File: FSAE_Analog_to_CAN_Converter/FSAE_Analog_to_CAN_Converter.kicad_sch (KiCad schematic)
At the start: 31 parts, among them J1 Conn_01x05_Pin, J2 Conn_01x08_Pin, J3 Conn_01x02_Pin, U1 STM32F103RCTx, U2 AP63205WU, U3 MCP2561-E-MF, U4 LT1962-3.3

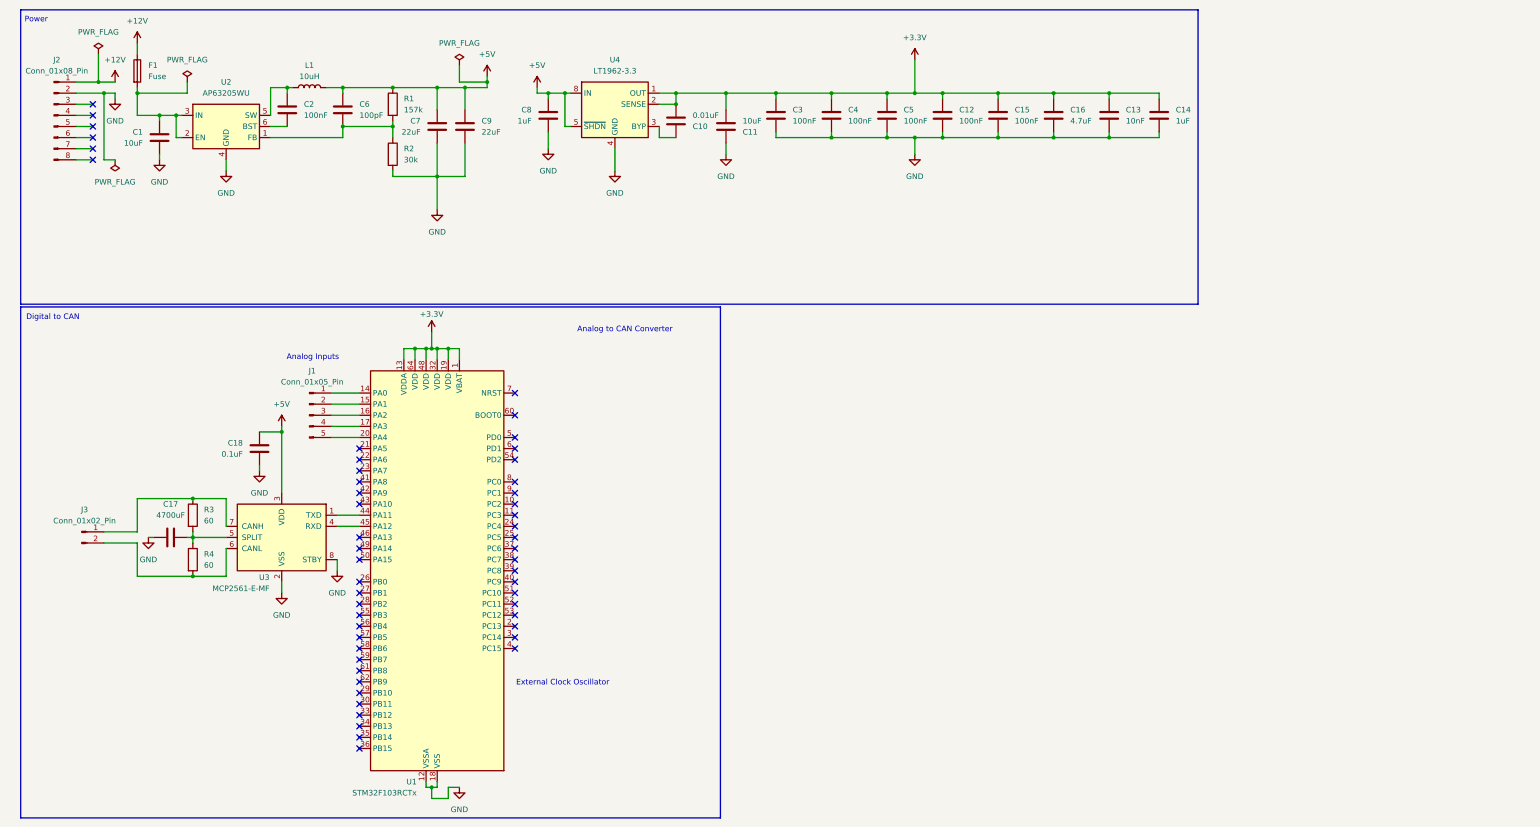
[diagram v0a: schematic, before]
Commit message: assigned footprints
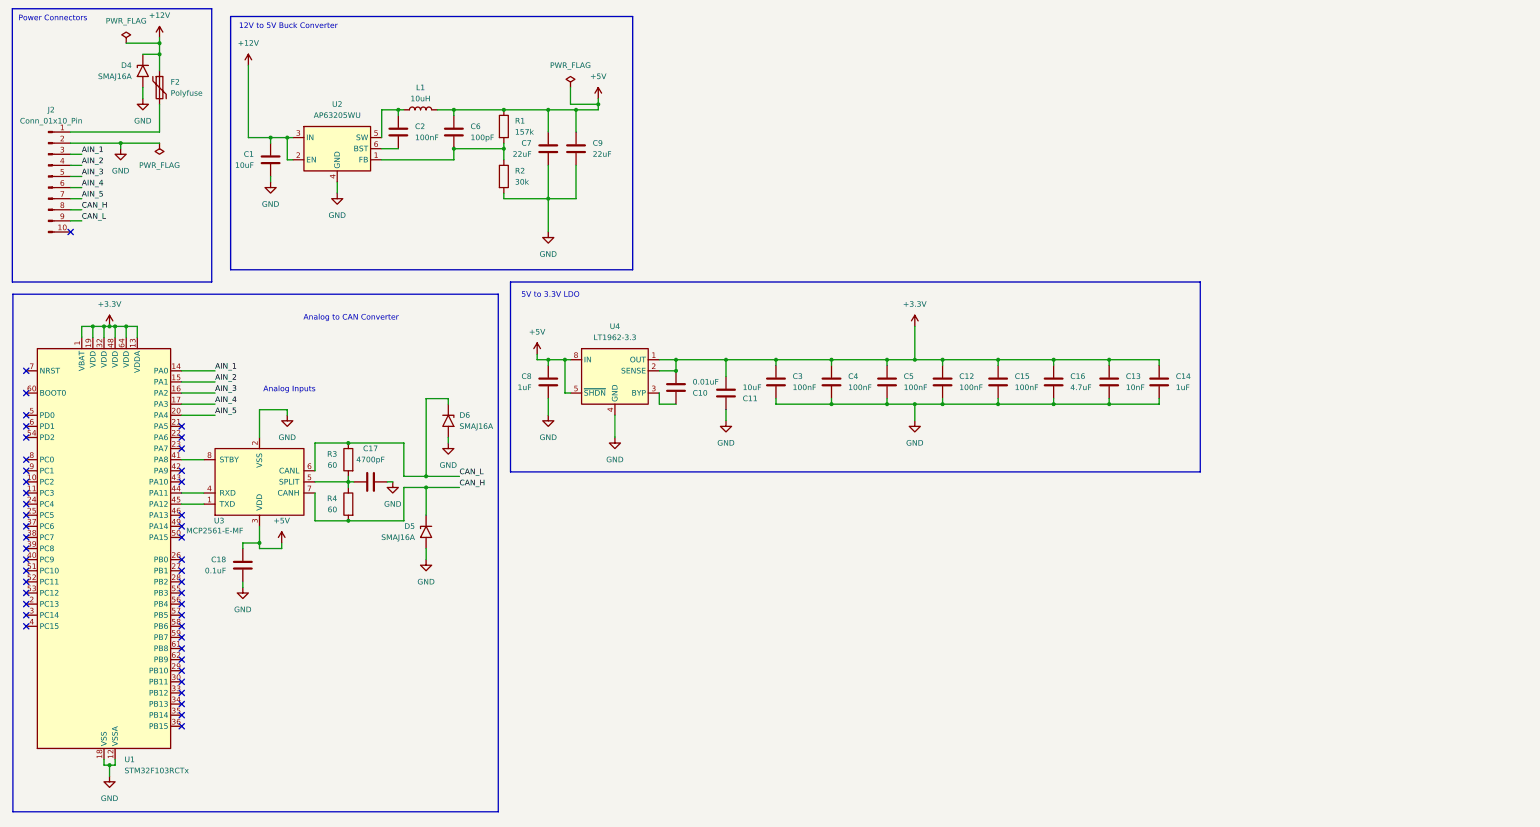
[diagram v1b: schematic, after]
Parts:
- removed F1: Fuse, symbol Device:Fuse
- removed J1: Conn_01x05_Pin, symbol Connector:Conn_01x05_Pin
- removed J2: Conn_01x08_Pin, symbol Connector:Conn_01x08_Pin
- removed J3: Conn_01x02_Pin, symbol Connector:Conn_01x02_Pin
- added D4, D5, D6: SMAJ16A, Diode_SMD:D_SMA, symbol Diode:SMAJ16A
- added F2: Polyfuse, Fuse:Fuse_1812_4532Metric_Pad1.30x3.40mm_HandSolder, symbol Device:Polyfuse
- added J2: Conn_01x10_Pin, Connector_Molex:Molex_KK-254_AE-6410-10A_1x10_P2.54mm_Vertical, symbol Connector:Conn_01x10_Pin
- C1, C10, C11, C12, C13, C14, C15, C16, C18, C2, C3, C4, C5, C6, C7, C8, C9: footprint (none) -> Capacitor_SMD:C_0603_1608Metric_Pad1.08x0.95mm_HandSolder
- C17: value 4700uF -> 4700pF; footprint (none) -> Capacitor_SMD:C_0603_1608Metric_Pad1.08x0.95mm_HandSolder
- L1: footprint (none) -> Inductor_SMD:L_0201_0603Metric_Pad0.64x0.40mm_HandSolder
- R1, R2, R3, R4: footprint (none) -> Resistor_SMD:R_0201_0603Metric_Pad0.64x0.40mm_HandSolder
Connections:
- net +12V: now also C1.1, U2.2 (EN), U2.3 (IN), D4.1 (A1), F2.1
- net GND: now also D4.2 (A2), D5.2 (A2), D6.2 (A2), J2.2 (Pin_2); no longer U3.8 (STBY)
- net CAN_H: now reaches U3.7 (CANH)
- net CAN_H: now also R4.2, D5.1 (A1), J2.8 (Pin_8); no longer R3.1
- net CAN_L: now reaches U3.6 (CANL)
- net CAN_L: now also R3.1, D6.1 (A1), J2.9 (Pin_9); no longer R4.2
- net AIN_1: now reaches U1.14 (PA0)
- net AIN_1: now also J2.3 (Pin_3)
- net AIN_2: now reaches U1.15 (PA1)
- net AIN_2: now also J2.4 (Pin_4)
- net AIN_3: now reaches U1.16 (PA2)
- net AIN_3: now also J2.5 (Pin_5)
- net AIN_4: now reaches U1.17 (PA3)
- net AIN_4: now also J2.6 (Pin_6)
- net AIN_5: now reaches U1.20 (PA4)
- net AIN_5: now also J2.7 (Pin_7)
- net at U1.41 (PA8): now also U3.8 (STBY)
- net at U1.44 (PA11): now also U3.4 (RXD); no longer U3.1 (TXD)
- net at U1.45 (PA12): now also U3.1 (TXD); no longer U3.4 (RXD)
- new net: F2.2, J2.1 (Pin_1)
- no-connect marks 52 -> 46
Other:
- note added: "12V to 5V Buck Converter"
- note added: "5V to 3.3V LDO"
- note added: "Power Connectors"
- note removed: "Digital to CAN"
- note removed: "External Clock Oscillator"
- note removed: "Power"
- moved on the sheet: C1, C10, C11, C12, C13, C14, C15, C16, C17, C18, C2, C3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

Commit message: started layout and traces
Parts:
- J1: renamed from J2; footprint Connector_Molex:Molex_KK-254_AE-6410-10A_1x10_P2.54mm_Vertical -> Connector_Molex:Molex_Mini-Fit_Jr_5566-10A_2x05_P4.20mm_Vertical
- L1: footprint Inductor_SMD:L_0201_0603Metric_Pad0.64x0.40mm_HandSolder -> Inductor_SMD:L_1210_3225Metric_Pad1.42x2.65mm_HandSolder
- renumbered C18 to C1, C11 to C10, C3 to C11, C4 to C12, C5 to C13, C12 to C14, C13 to C17, C14 to C18, C1 to C2, C17 to C3, C2 to C4, C6 to C5, C7 to C6, C8 to C7, C9 to C8, C10 to C9, D4 to D1, D5 to D2, D6 to D3, F2 to F1, R3 to R1, R4 to R2, R1 to R3, R2 to R4, U3 to U2, U2 to U3

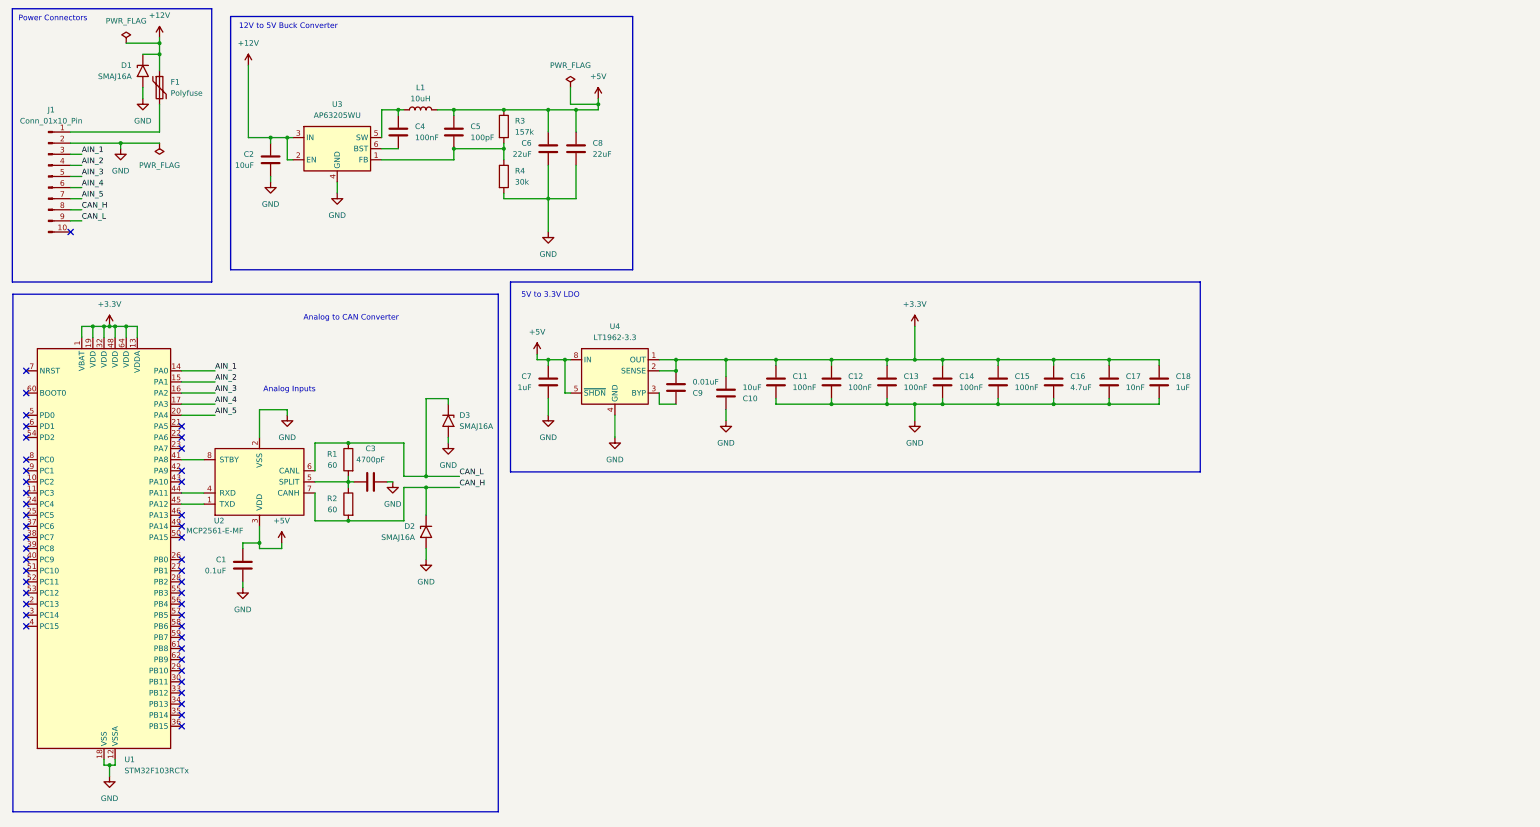
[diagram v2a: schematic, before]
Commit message: added external clock, and SWD output header
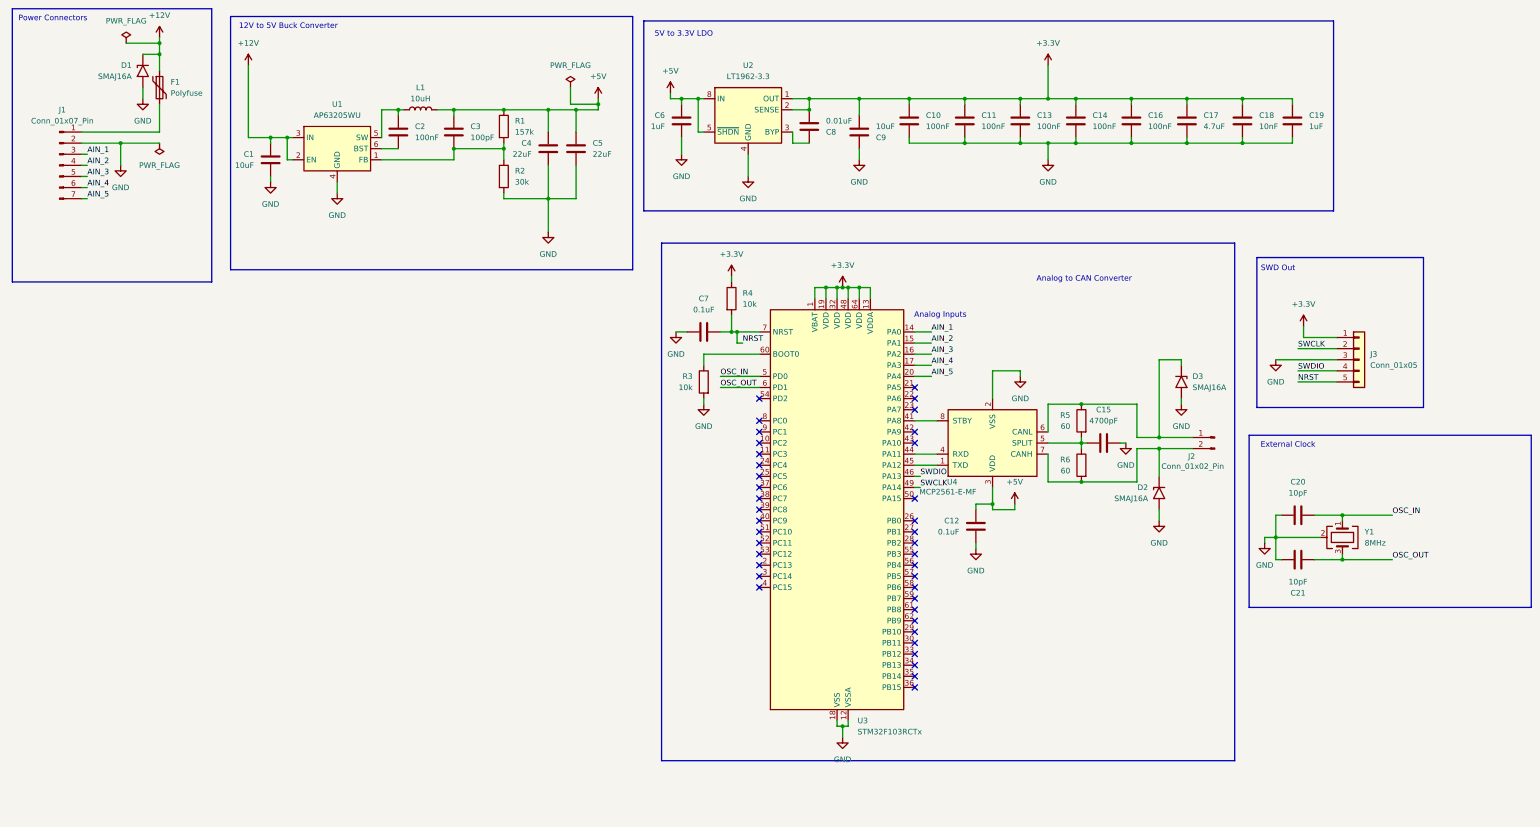
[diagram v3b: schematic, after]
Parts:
- removed J1: Conn_01x10_Pin, Connector_Molex:Molex_Mini-Fit_Jr_5566-10A_2x05_P4.20mm_Vertical, symbol Connector:Conn_01x10_Pin
- added C20, C21: 10pF, Capacitor_SMD:C_0603_1608Metric_Pad1.08x0.95mm_HandSolder, symbol Device:C
- added C7: 0.1uF, Capacitor_SMD:C_0603_1608Metric_Pad1.08x0.95mm_HandSolder, symbol Device:C
- added J1: Conn_01x07_Pin, Connector_Molex:Molex_Micro-Fit_3.0_43650-0700_1x07_P3.00mm_Horizontal, symbol Connector:Conn_01x07_Pin
- added J2: Conn_01x02_Pin, Connector_Molex:Molex_Micro-Fit_3.0_43650-0200_1x02_P3.00mm_Horizontal, symbol Connector:Conn_01x02_Pin
- added J3: Conn_01x05, Connector_PinHeader_2.54mm:PinHeader_1x05_P2.54mm_Vertical, symbol Connector_Generic:Conn_01x05
- added R3, R4: 10k, Resistor_SMD:R_0201_0603Metric_Pad0.64x0.40mm_HandSolder, symbol Device:R
- added Y1: 8MHz, Crystal:Crystal_SMD_3225-4Pin_3.2x2.5mm_HandSoldering, symbol Device:Crystal_GND24
- renumbered C2 to C1, C11 to C10, C12 to C11, C1 to C12, C3 to C15, C15 to C16, C16 to C17, C17 to C18, C18 to C19, C4 to C2, C5 to C3, C6 to C4, C8 to C5, C7 to C6, C9 to C8, C10 to C9, R3 to R1, R4 to R2, R1 to R5, R2 to R6, U3 to U1, U4 to U2, U1 to U3, U2 to U4
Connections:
- net +3.3V: now also J3.1 (Pin_1), R4.1
- net AIN_1: now also J1.3 (Pin_3)
- net AIN_2: now also J1.4 (Pin_4)
- net AIN_3: now also J1.5 (Pin_5)
- net AIN_4: now also J1.6 (Pin_6)
- net AIN_5: now also J1.7 (Pin_7)
- net GND: now also C20.1, C21.1, C7.1, J1.2 (Pin_2), J3.3 (Pin_3), R3.2, Y1.2 (G), Y1.4 (G)
- net SWDIO: now reaches U3.46 (PA13)
- net SWDIO: now also J3.4 (Pin_4)
- net SWCLK: now reaches U3.49 (PA14)
- net SWCLK: now also J3.2 (Pin_2)
- net OSC_IN: now reaches U3.5 (PD0)
- net OSC_IN: now also C20.2, Y1.1
- net OSC_OUT: now reaches U3.6 (PD1)
- net OSC_OUT: now also C21.2, Y1.3
- net at U3.60 (BOOT0): now also R3.1
- net NRST: now reaches U3.7 (NRST)
- net NRST: now also C7.2, J3.5 (Pin_5), R4.2
- net at F1.2: now also J1.1 (Pin_1)
- net CAN_H: no longer names the net of D2.1 (A1), R6.2, U4.7 (CANH)
- net CAN_H: now also J2.2 (Pin_2)
- net CAN_L: no longer names the net of D3.1 (A1), R5.1, U4.6 (CANL)
- net CAN_L: now also J2.1 (Pin_1)
- no-connect marks 46 -> 39
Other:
- note added: "External Clock"
- note added: "SWD Out"
- moved on the sheet: C10, C11, C12, C13, C14, C15, C16, C17, C18, C19, C6, C8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

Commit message: removed uneccesary stuff
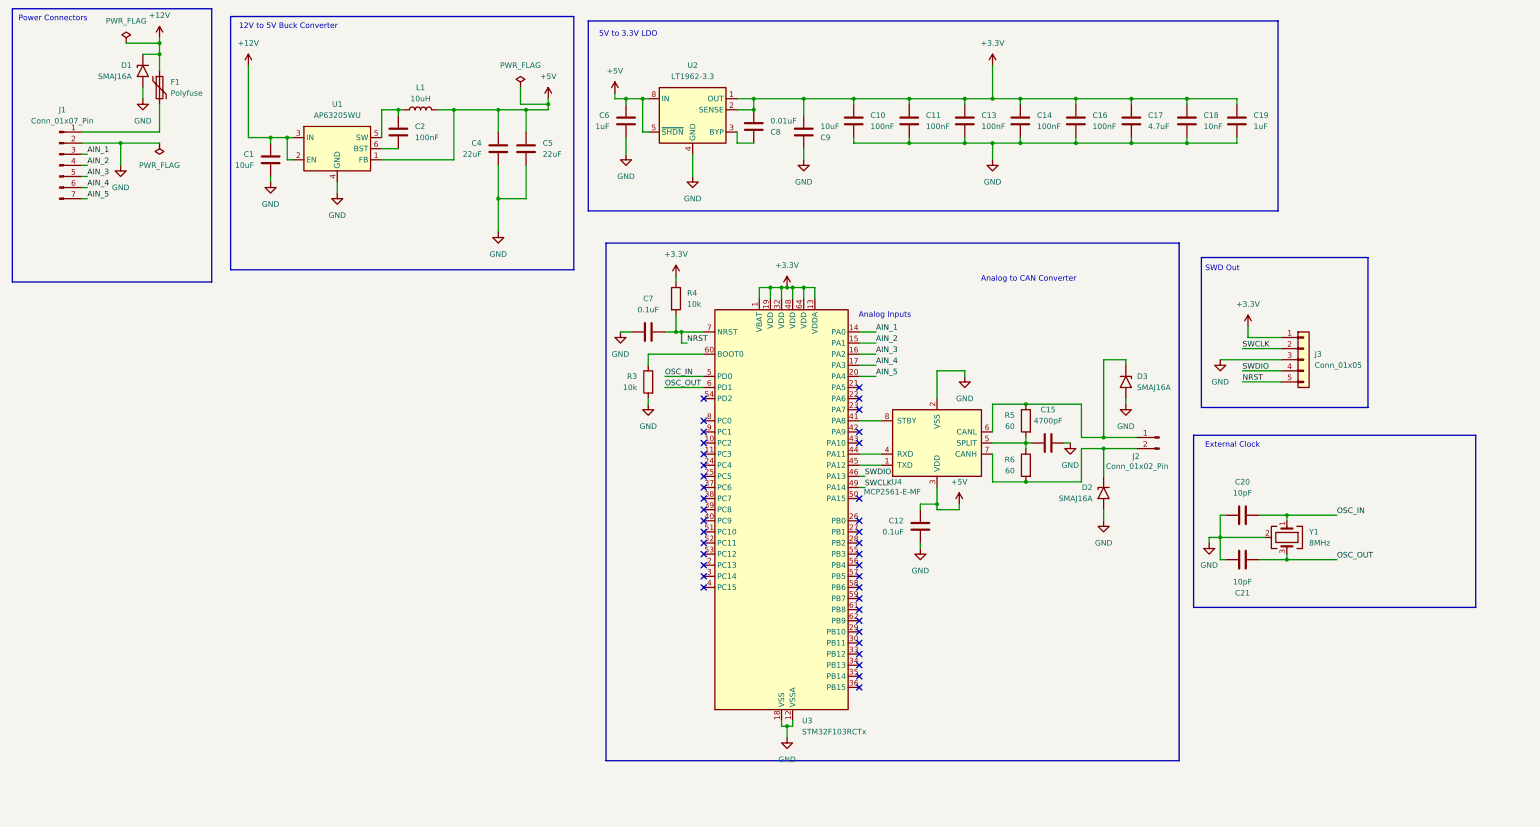
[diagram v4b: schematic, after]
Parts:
- removed C3: 100pF, Capacitor_SMD:C_0603_1608Metric_Pad1.08x0.95mm_HandSolder, symbol Device:C
- removed R1: 157k, Resistor_SMD:R_0201_0603Metric_Pad0.64x0.40mm_HandSolder, symbol Device:R
- removed R2: 30k, Resistor_SMD:R_0201_0603Metric_Pad0.64x0.40mm_HandSolder, symbol Device:R
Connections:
- net +5V: now also U1.1 (FB)
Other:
- moved on the sheet: C10, C11, C12, C13, C14, C15, C16, C17, C18, C19, C20, C21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

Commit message: almost done
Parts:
- removed C12: 0.1uF, Capacitor_SMD:C_0603_1608Metric_Pad1.08x0.95mm_HandSolder, symbol Device:C
- removed C15: 4700pF, Capacitor_SMD:C_0603_1608Metric_Pad1.08x0.95mm_HandSolder, symbol Device:C
- removed D2, D3: SMAJ16A, Diode_SMD:D_SMA, symbol Diode:SMAJ16A
- removed R4: 10k, Resistor_SMD:R_0201_0603Metric_Pad0.64x0.40mm_HandSolder, symbol Device:R
- removed R5, R6: 60, Resistor_SMD:R_0201_0603Metric_Pad0.64x0.40mm_HandSolder, symbol Device:R
- removed U4: MCP2561-E-MF, Package_DFN_QFN:DFN-8-1EP_3x3mm_P0.65mm_EP1.55x2.4mm, symbol Interface_CAN_LIN:MCP2561-E-MF
- removed Y1: 8MHz, Crystal:Crystal_SMD_3225-4Pin_3.2x2.5mm_HandSoldering, symbol Device:Crystal_GND24
- added C11, C13: 100nF, Capacitor_SMD:C_0603_1608Metric_Pad1.08x0.95mm_HandSolder, symbol Device:C
- added U4: MCP2562-E-MF, Package_DFN_QFN:DFN-8-1EP_3x3mm_P0.65mm_EP1.55x2.4mm, symbol Interface_CAN_LIN:MCP2562-E-MF
- added Y1: 8MHz, Crystal:Crystal_SMD_2012-2Pin_2.0x1.2mm_HandSoldering, symbol Device:Crystal
- J2: footprint Connector_Molex:Molex_Micro-Fit_3.0_43650-0200_1x02_P3.00mm_Horizontal -> Connector_Molex:Molex_Micro-Fit_3.0_43045-0212_2x01_P3.00mm_Vertical
- renumbered C11 to C10, C13 to C12, C16 to C15, C17 to C16, C18 to C17, C19 to C18, C20 to C19, C21 to C20, C4 to C3, C5 to C4, C6 to C5, C7 to C6, C8 to C7, C9 to C8, C10 to C9, R3 to R1
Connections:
- net +3.3V: now also C11.2, U4.5 (Vio), U4.8 (SHDN)
- net +5V: now also C13.2, U4.3 (VDD)
- net AIN_1: now also U3.23 (PA7); no longer U3.14 (PA0)
- net AIN_2: now also U3.24 (PC4); no longer U3.15 (PA1)
- net AIN_3: now also U3.25 (PC5); no longer U3.16 (PA2)
- net AIN_4: now also U3.26 (PB0); no longer U3.17 (PA3)
- net AIN_5: now also U3.27 (PB1); no longer U3.20 (PA4)
- net GND: now also C11.1, C13.1, U4.2 (VSS), U4.9 (PAD)
- net CAN_OUT_P: now reaches J2.1 (Pin_1)
- net CAN_OUT_P: now also U4.7 (CANH)
- net CAN_OUT_N: now reaches J2.2 (Pin_2)
- net CAN_OUT_N: now also U4.6 (CANL)
- net CAN_RX: now reaches U3.44 (PA11)
- net CAN_RX: now also U4.4 (RXD)
- net CAN_TX: now reaches U3.45 (PA12)
- net CAN_TX: now also U4.1 (TXD)
- net OSC_IN renamed OSC_P
- net OSC_P: now also Y1.2
- net OSC_OUT renamed OSC_N
- net OSC_N: now also Y1.1
- no-connect marks 39 -> 40
